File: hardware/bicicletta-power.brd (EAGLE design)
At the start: 160 x 100 mm, 23 parts, among them IC1 LM5017, IC2 LM1117-3.3

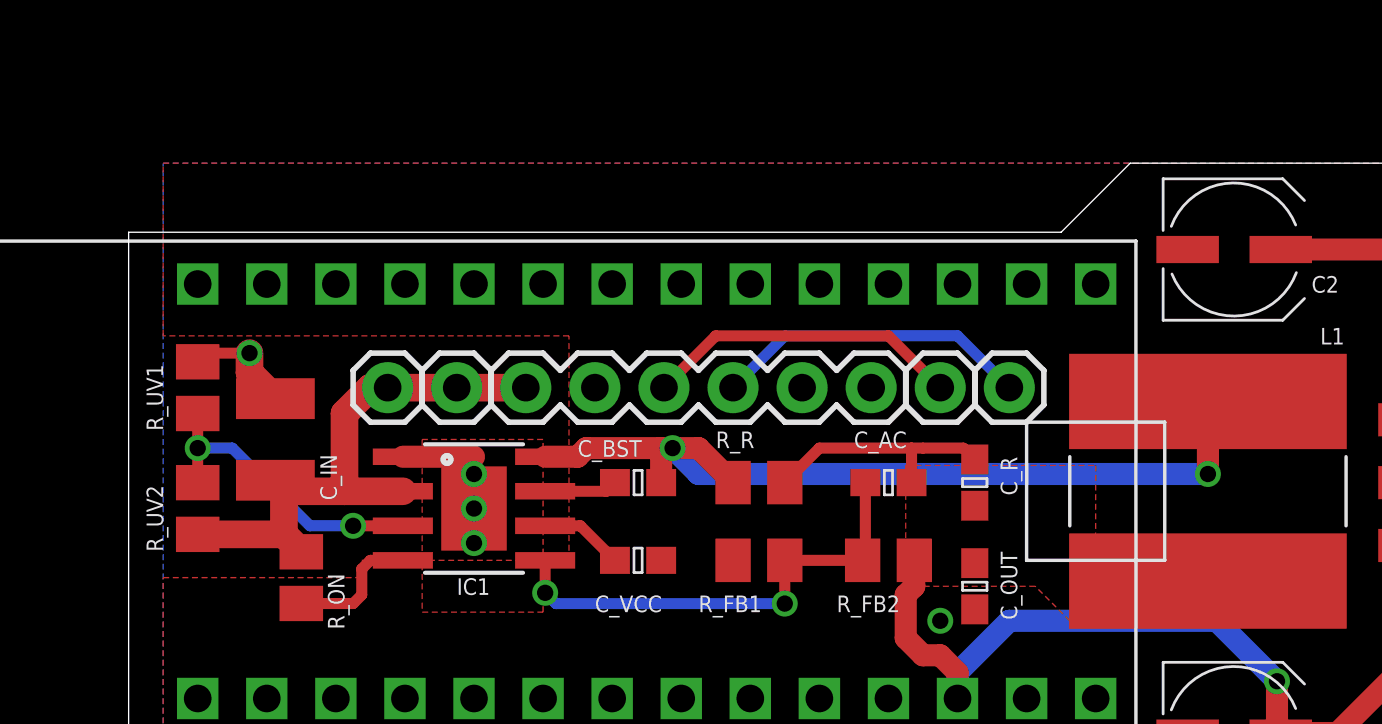
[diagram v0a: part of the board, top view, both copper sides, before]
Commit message: Futzing with the ground planes and via tenting.
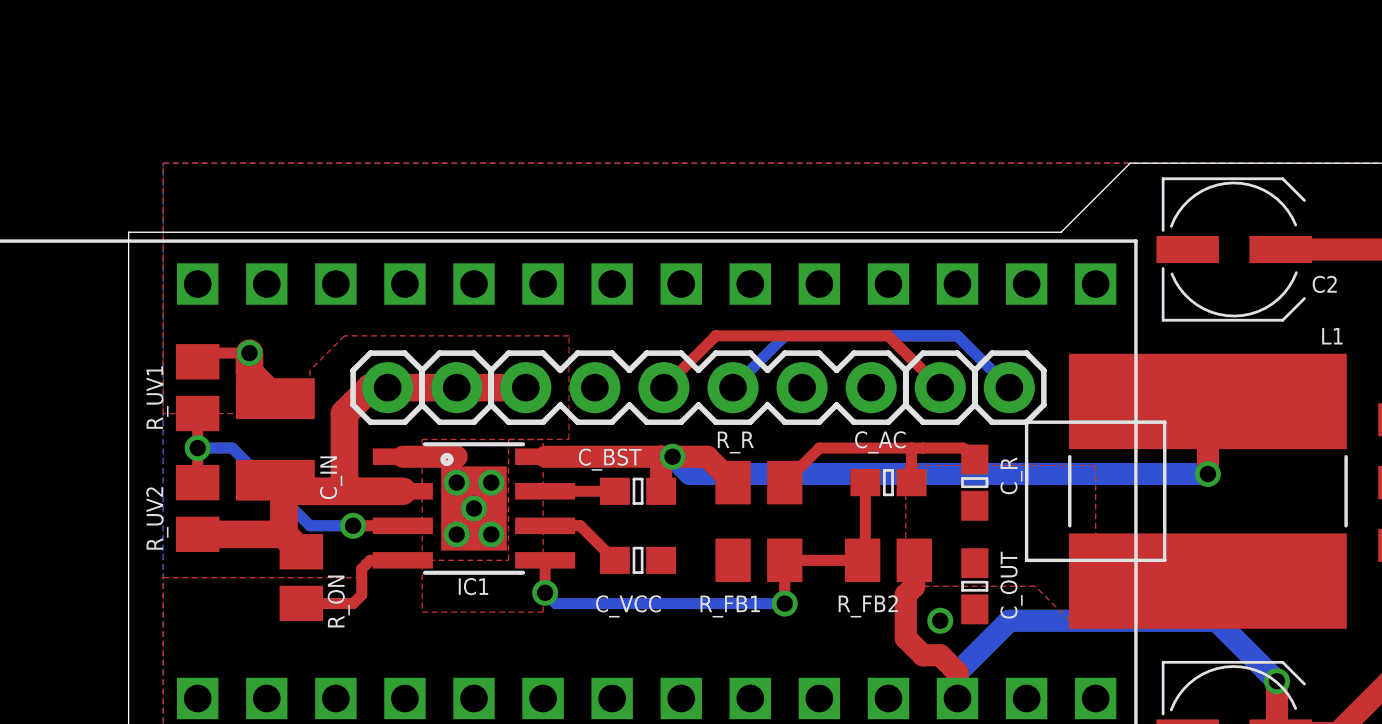
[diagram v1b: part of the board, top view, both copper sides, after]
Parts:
- moved C_BST 0.32 mm to (59.4, 74.3)
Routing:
- net N$4: track 32.0 -> 31.2 mm
- net GND: track 7.55 -> 7.23 mm, vias 5 -> 7
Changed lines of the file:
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@@
 <param name="mlMinCreamFrame" value="0mil"/>
 <param name="mlMaxCreamFrame" value="0mil"/>
-<param name="mlViaStopLimit" value="0mil"/>
+<param name="mlViaStopLimit" value="25mil"/>
 <param name="srRoundness" value="0"/>
 <param name="srMinRoundness" value="0mil"/>
@@
 <attribute name="VALUE" x="58.7375" y="69.85" size="1.27" layer="27"/>
 </element>
-<element name="C_BST" library="rcl" package="C0603" value="0.01uF" x="59.3725" y="74.6125" smashed="yes">
-<attribute name="NAME" x="57.15" y="75.565" size="0.6096" layer="25"/>
-<attribute name="VALUE" x="58.7375" y="72.7075" size="1.27" layer="27"/>
+<element name="C_BST" library="rcl" package="C0603" value="0.01uF" x="59.3725" y="74.295" smashed="yes">
+<attribute name="NAME" x="57.15" y="75.2475" size="0.6096" layer="25"/>
+<attribute name="VALUE" x="58.7375" y="72.39" size="1.27" layer="27"/>
 </element>
 <element name="C_IN" library="rcl" package="C1210K" value="2.2uF" x="46.0375" y="76.2" smashed="yes" rot="R90">
@@
 <contactref element="C1" pad="-"/>
 <contactref element="JP3" pad="2"/>
-<polygon width="0.4064" layer="16">
+<polygon width="0.4064" layer="16" isolate="0.3048">
 <vertex x="41.91" y="86.36"/>
 <vertex x="96.52" y="86.36"/>
@@
 <vertex x="41.91" y="62.23"/>
 </polygon>
-<polygon width="0.4064" layer="1" isolate="0.254" rank="2">
+<polygon width="0.4064" layer="1" isolate="0.3048" rank="2">
 <vertex x="41.91" y="86.36"/>
 <vertex x="96.52" y="86.36"/>
@@
 <vertex x="49.2125" y="71.12"/>
 <vertex x="49.2125" y="71.755"/>
-<vertex x="56.8325" y="71.755"/>
+<vertex x="54.61" y="71.755"/>
+<vertex x="54.61" y="76.2"/>
+<vertex x="56.8325" y="76.2"/>
 <vertex x="56.8325" y="80.01"/>
-<vertex x="41.91" y="80.01"/>
+<vertex x="48.5775" y="80.01"/>
+<vertex x="47.3075" y="78.74"/>
+<vertex x="47.3075" y="77.1525"/>
+<vertex x="41.91" y="77.1525"/>
 </polygon>
 <via x="53.34" y="73.66" extent="1-16" drill="0.6"/>
-<via x="53.34" y="72.39" extent="1-16" drill="0.6"/>
-<via x="53.34" y="74.93" extent="1-16" drill="0.6"/>
-<wire x1="50.7238" y1="75.565" x2="53.34" y2="75.565" width="0.8128" layer="1"/>
-<wire x1="53.34" y1="75.565" x2="53.34" y2="74.93" width="0.3048" layer="1"/>
+<via x="52.705" y="72.7075" extent="1-16" drill="0.6"/>
+<via x="52.705" y="74.6125" extent="1-16" drill="0.6"/>
+<wire x1="50.7238" y1="75.565" x2="52.705" y2="75.565" width="0.8128" layer="1"/>
+<wire x1="52.705" y1="75.565" x2="52.705" y2="74.6125" width="0.3048" layer="1"/>
 <via x="70.485" y="69.5325" extent="1-16" drill="0.6"/>
 <via x="45.085" y="79.375" extent="1-16" drill="0.6"/>
@@
 <vertex x="51.435" y="76.2"/>
 </polygon>
+<via x="53.975" y="72.7075" extent="1-16" drill="0.6"/>
+<via x="53.975" y="74.6125" extent="1-16" drill="0.6"/>
 </signal>
 <signal name="V_BATT">
@@
 <contactref element="R_R" pad="1"/>
 <contactref element="C_BST" pad="2"/>
-<wire x1="55.9562" y1="75.565" x2="57.15" y2="75.565" width="0.8128" layer="1"/>
-<wire x1="57.15" y1="75.565" x2="57.4675" y2="75.8825" width="0.8128" layer="1"/>
-<wire x1="57.4675" y1="75.8825" x2="60.6425" y2="75.8825" width="0.8128" layer="1"/>
-<via x="60.6425" y="75.8825" extent="1-16" drill="0.6"/>
-<wire x1="60.2225" y1="74.6125" x2="60.2225" y2="75.8825" width="0.8128" layer="1"/>
-<wire x1="60.2225" y1="75.8825" x2="60.6425" y2="75.8825" width="0.8128" layer="1"/>
+<wire x1="55.9562" y1="75.565" x2="60.2225" y2="75.565" width="0.8128" layer="1"/>
+<via x="60.6425" y="75.565" extent="1-16" drill="0.6"/>
+<wire x1="60.2225" y1="74.295" x2="60.2225" y2="75.565" width="0.8128" layer="1"/>
+<wire x1="60.2225" y1="75.565" x2="60.6425" y2="75.565" width="0.8128" layer="1"/>
 <wire x1="80.3275" y1="77.597" x2="80.3275" y2="74.93" width="0.8128" layer="1"/>
 <via x="80.3275" y="74.93" extent="1-16" drill="0.6"/>
-<wire x1="80.3275" y1="74.93" x2="61.595" y2="74.93" width="0.8128" layer="16"/>
-<wire x1="61.595" y1="74.93" x2="60.6425" y2="75.8825" width="0.8128" layer="16"/>
-<wire x1="60.6425" y1="75.8825" x2="61.5975" y2="75.8825" width="0.8128" layer="1"/>
-<wire x1="61.5975" y1="75.8825" x2="62.8675" y2="74.6125" width="0.8128" layer="1"/>
+<wire x1="80.3275" y1="74.93" x2="61.2775" y2="74.93" width="0.8128" layer="16"/>
+<wire x1="61.2775" y1="74.93" x2="60.6425" y2="75.565" width="0.8128" layer="16"/>
+<wire x1="60.6425" y1="75.565" x2="61.915" y2="75.565" width="0.8128" layer="1"/>
+<wire x1="61.915" y1="75.565" x2="62.8675" y2="74.6125" width="0.8128" layer="1"/>
 </signal>
 <signal name="N$6">
@@
 <contactref element="IC1" pad="7"/>
 <contactref element="C_BST" pad="1"/>
-<wire x1="55.9562" y1="74.295" x2="58.205" y2="74.295" width="0.4064" layer="1"/>
-<wire x1="58.205" y1="74.295" x2="58.5225" y2="74.6125" width="0.4064" layer="1"/>
+<wire x1="55.9562" y1="74.295" x2="58.5225" y2="74.295" width="0.4064" layer="1"/>
 </signal>
 <signal name="N$9">

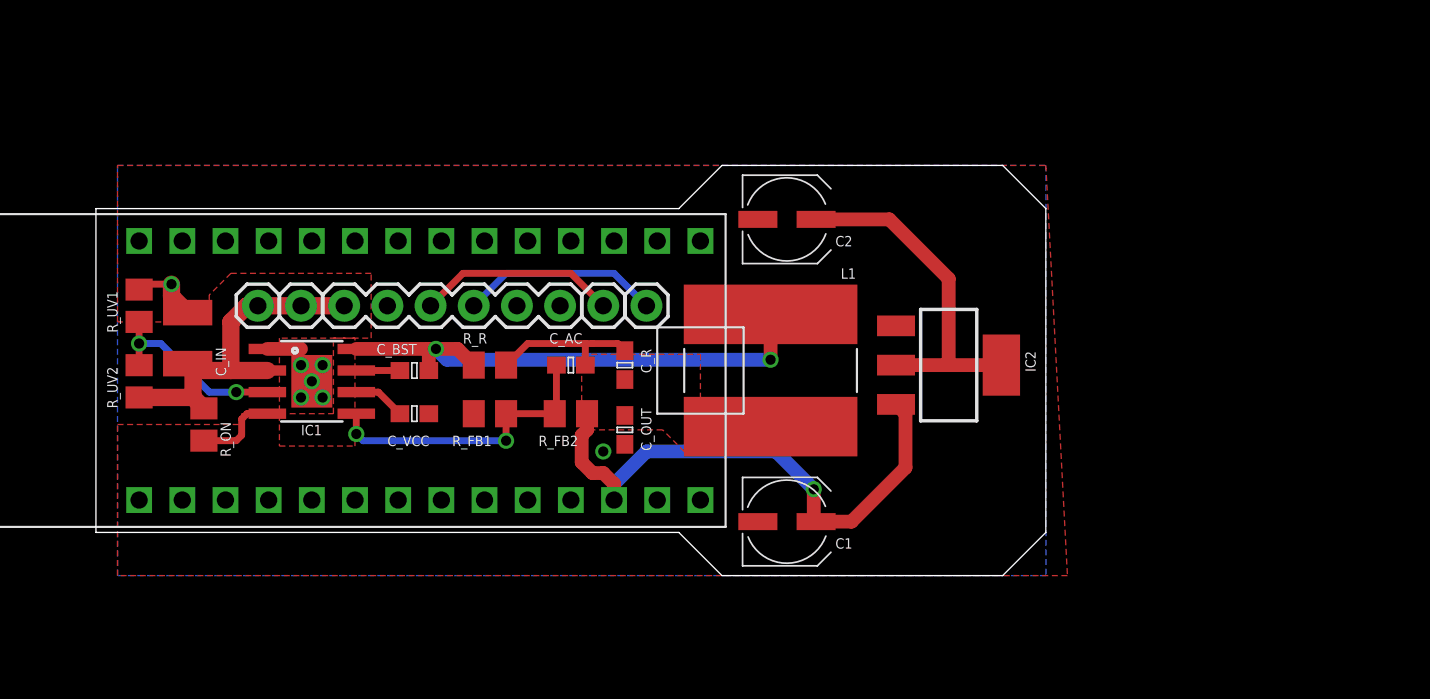
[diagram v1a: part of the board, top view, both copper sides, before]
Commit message: To hell with the buck regulator, let's just take 5V from the controller.
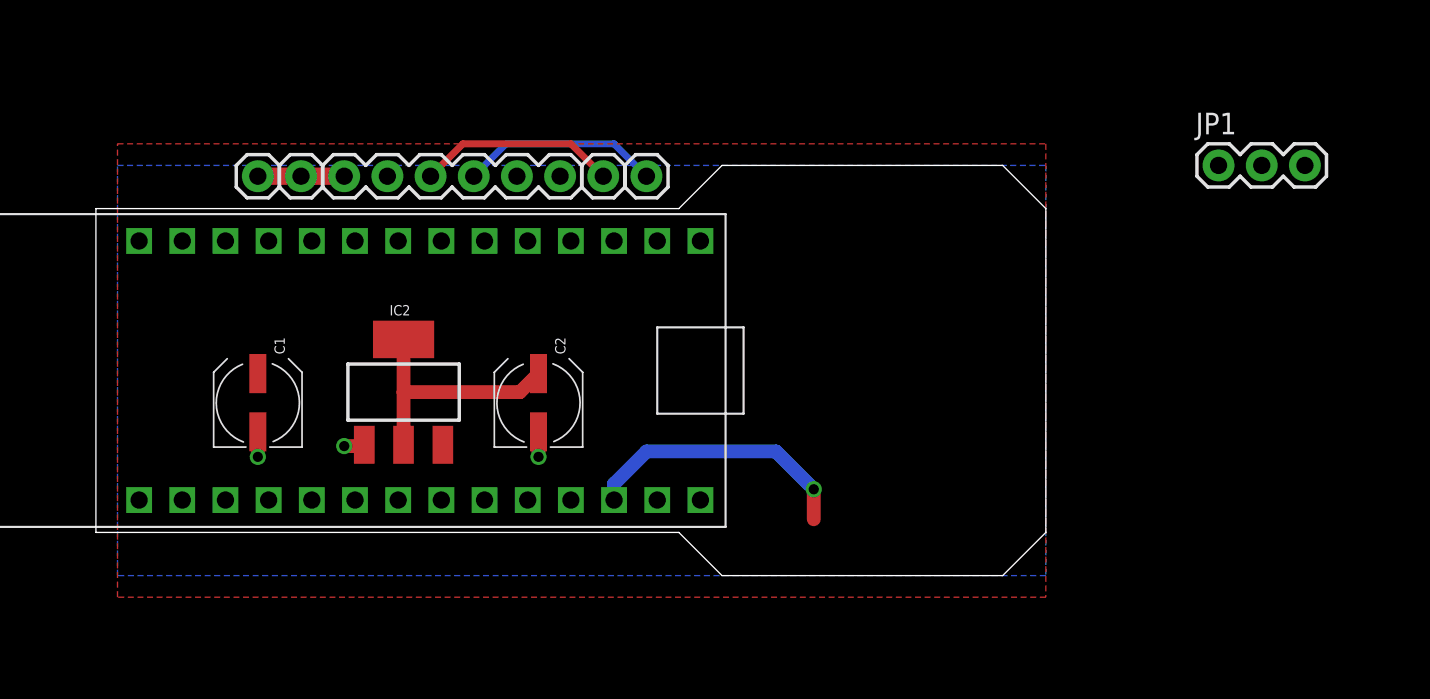
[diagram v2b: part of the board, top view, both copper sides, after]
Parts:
- removed C_AC: 100nF, rcl:C0603
- removed C_BST: 0.01uF, rcl:C0603
- removed C_IN: 2.2uF, rcl:C1210K
- removed C_OUT: 5.6uF, rcl:C0603
- removed C_R: 3300pF, rcl:C0603
- removed C_VCC: 1uF, rcl:C0603
- removed IC1: LM5017, Railstars:SOIC-8-POWERPAD
- removed L1: 100uH, Railstars:SRN1060
- removed R_FB1: 1K, rcl:M0805
- removed R_FB2: 3K, rcl:M0805
- removed R_ON: 250K, rcl:M0805
- removed R_R: 2M, rcl:M0805
- removed R_UV1: 14K, rcl:M0805
- removed R_UV2: 125K, rcl:M0805
- added JP1: (no value), SparkFun-Connectors:1X03
- moved IC2 32.1 mm to (58.7, 73.0), turned to 0 degrees
- moved C1 31.9 mm to (50.2, 72.4), turned to 90 degrees
- moved C2 18.2 mm to (66.7, 72.4), turned to 90 degrees
- moved JP3 7.62 mm to (55.2, 85.7)
- moved JP4 7.62 mm to (73.0, 85.7)
- moved JP5 7.62 mm to (70.5, 85.7)
- moved JP6 7.62 mm to (50.2, 85.7)
- moved JP7 7.62 mm to (52.7, 85.7)
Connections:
- removed net N$1: IC1.4, R_ON.2
- removed net N$2: C_AC.2, IC1.5, R_FB1.2, R_FB2.1
- removed net N$3: IC1.3, R_UV1.2, R_UV2.2
- removed net N$4: C_BST.2, IC1.8, L1.P$1, R_R.1
- removed net N$6: C_AC.1, C_R.1, R_R.2
- removed net N$7: C_BST.1, IC1.7
- removed net N$9: C_VCC.1, IC1.6
- net 5V: no longer C_OUT.1, C_R.2, L1.P$2, R_FB2.2
- net GND: no longer C_IN.2, C_OUT.2, C_VCC.2, IC1.1, IC1.P$1, R_FB1.1, R_UV1.1
- net V_BATT: no longer C_IN.1, IC1.2, R_ON.1, R_UV2.1
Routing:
- net N$4: track 31.2 -> 0.00 mm, vias 2 -> 0
- net N$2: track 17.5 -> 0.00 mm, vias 2 -> 0
- net 5V: track 33.4 -> 16.2 mm
- net V_BATT: track 21.0 -> 5.08 mm
- net N$3: track 11.3 -> 0.00 mm, vias 2 -> 0
- net N$6: track 8.96 -> 0.00 mm
- net 3.3V: track 20.5 -> 14.6 mm
- net N$1: track 4.95 -> 0.00 mm
- net N$9: track 3.09 -> 0.00 mm
- net GND: track 7.23 -> 4.16 mm, vias 7 -> 3
- net N$7: track 2.57 -> 0.00 mm
- removed copper zone on layer 1, net GND

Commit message: Revert "To hell with the buck regulator, let's just take 5V from the controller."
This reverts commit f16ee5c0247fff79c0027ea9109af273bc1d2e81.
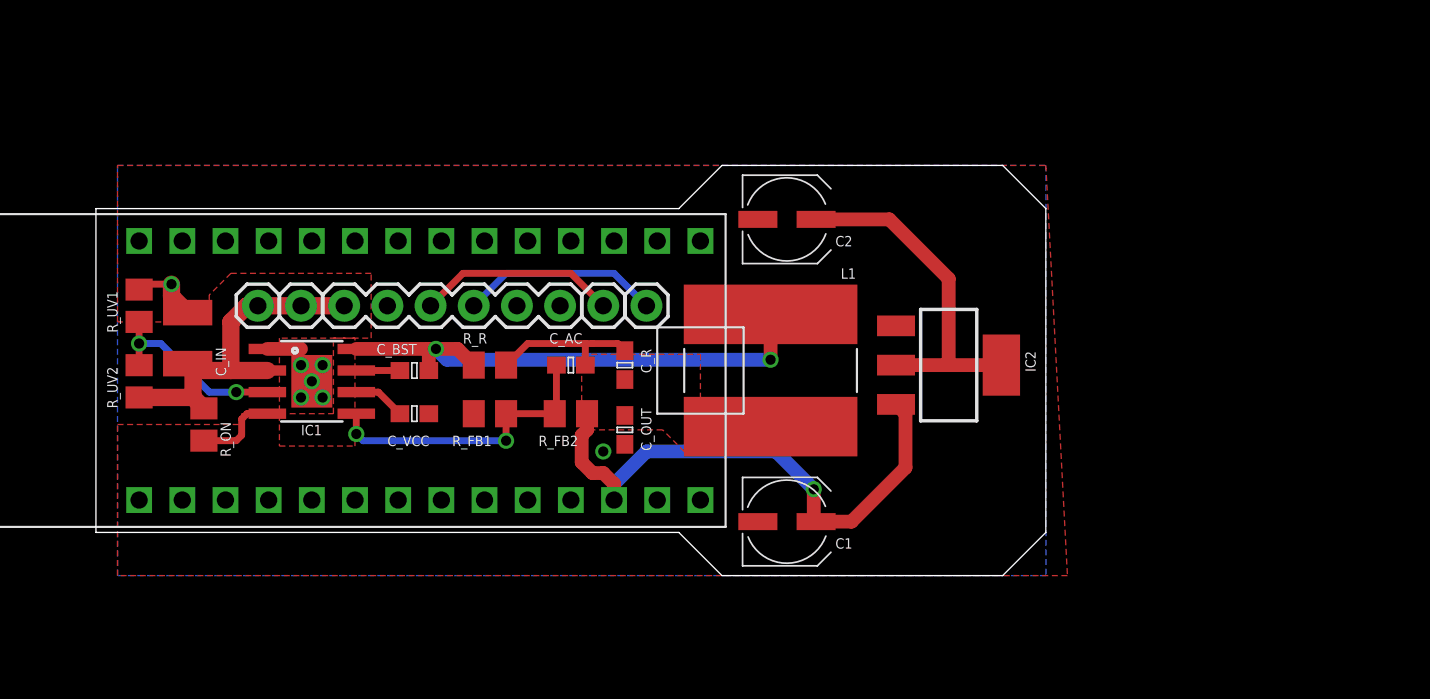
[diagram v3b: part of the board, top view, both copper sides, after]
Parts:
- removed JP1: (no value), SparkFun-Connectors:1X03
- added C_AC: 100nF, rcl:C0603
- added C_BST: 0.01uF, rcl:C0603
- added C_IN: 2.2uF, rcl:C1210K
- added C_OUT: 5.6uF, rcl:C0603
- added C_R: 3300pF, rcl:C0603
- added C_VCC: 1uF, rcl:C0603
- added IC1: LM5017, Railstars:SOIC-8-POWERPAD
- added L1: 100uH, Railstars:SRN1060
- added R_FB1: 1K, rcl:M0805
- added R_FB2: 3K, rcl:M0805
- added R_ON: 250K, rcl:M0805
- added R_R: 2M, rcl:M0805
- added R_UV1: 14K, rcl:M0805
- added R_UV2: 125K, rcl:M0805
- moved IC2 32.1 mm to (90.8, 74.6), turned to 270 degrees
- moved C1 31.9 mm to (81.3, 65.4), turned to 0 degrees
- moved C2 18.2 mm to (81.3, 83.2), turned to 0 degrees
- moved JP3 7.62 mm to (55.2, 78.1)
- moved JP4 7.62 mm to (73.0, 78.1)
- moved JP5 7.62 mm to (70.5, 78.1)
- moved JP6 7.62 mm to (50.2, 78.1)
- moved JP7 7.62 mm to (52.7, 78.1)
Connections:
- new net N$1: IC1.4, R_ON.2
- new net N$2: C_AC.2, IC1.5, R_FB1.2, R_FB2.1
- new net N$3: IC1.3, R_UV1.2, R_UV2.2
- new net N$4: C_BST.2, IC1.8, L1.P$1, R_R.1
- new net N$6: C_AC.1, C_R.1, R_R.2
- new net N$7: C_BST.1, IC1.7
- new net N$9: C_VCC.1, IC1.6
- net 5V: now also C_OUT.1, C_R.2, L1.P$2, R_FB2.2
- net GND: now also C_IN.2, C_OUT.2, C_VCC.2, IC1.1, IC1.P$1, R_FB1.1, R_UV1.1
- net V_BATT: now also C_IN.1, IC1.2, R_ON.1, R_UV2.1
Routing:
- net N$4: track 0.00 -> 31.2 mm, vias 0 -> 2
- net N$2: track 0.00 -> 17.5 mm, vias 0 -> 2
- net 5V: track 16.2 -> 33.4 mm
- net V_BATT: track 5.08 -> 21.0 mm
- net N$3: track 0.00 -> 11.3 mm, vias 0 -> 2
- net N$6: track 0.00 -> 8.96 mm
- net 3.3V: track 14.6 -> 20.5 mm
- net N$1: track 0.00 -> 4.95 mm
- net N$9: track 0.00 -> 3.09 mm
- net GND: track 4.16 -> 7.23 mm, vias 3 -> 7
- net N$7: track 0.00 -> 2.57 mm
- added copper zone on layer 1, net GND
